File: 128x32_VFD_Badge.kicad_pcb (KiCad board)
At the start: 2 copper layers, 94 x 34.3 mm, 71 parts, among them J1 USB_C_Receptacle_USB2.0_16P, J2 Micro_SD_Card_Det2, Q1 CMSN3416K-HF, Q2 CMSN3416K-HF, SW1 SKRKAEE020, SW2 SKRKAEE020, SW3 SKRKAEE020, U1 USBLC6-2SC6, U2 TPS61391, U3 SN6507DGQ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

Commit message: Rev 0.1
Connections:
- D2 pad 1: (no net) -> GND
- D2 pad 2: GND -> (no net)
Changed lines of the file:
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@@
 			(layers "B.Cu" "B.Paste" "B.Mask")
 			(roundrect_rratio 0.25)
+			(net 1 "GND")
+			(pinfunction "A")
+			(pintype "passive")
 		)
 		(pad "2" smd roundrect
@@
 			(layers "B.Cu" "B.Paste" "B.Mask")
 			(roundrect_rratio 0.25)
-			(net 1 "GND")
-			(pinfunction "A")
-			(pintype "passive")
 		)
 		(pad "3" smd roundrect

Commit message: bitbanging
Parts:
- turned TR1 to 90 degrees
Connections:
- TR1 pad 1: /Controller & Display/Filament Driver/F1 -> Net-(U3-SW1)
- TR1 pad 2: Net-(D2-K) -> +3.3V
- TR1 pad 3: Net-(R8-Pad1) -> Net-(U3-SW2)
- TR1 pad 4: Net-(U3-SW1) -> /Controller & Display/Filament Driver/F1
- TR1 pad 5: +3.3V -> Net-(D2-K)
- TR1 pad 6: Net-(U3-SW2) -> Net-(R8-Pad1)
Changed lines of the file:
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@@
 		(property "Value" "+"
 			(at 4 -7 0)
-			(layer "B.Fab")
+			(layer "B.SilkS")
 			(effects
 				(font
@@
 		(property "Value" "-"
 			(at 4 -7 0)
-			(layer "B.Fab")
+			(layer "B.SilkS")
 			(effects
 				(font
@@
 	(footprint "Noritake:Transformer_Wuerth_750316888"
 		(layer "B.Cu")
-		(at 214.4 82 -90)
+		(at 214.4 82 90)
 		(descr "Power Transformer, horizontal core with bobbin, 6 pin, 2.54mm pitch, 11.24mm row spacing, 12.6x8.3x4.1mm")
 		(tags "transformer flyback")
@@
 		)
 		(property "Footprint" "Noritake:Transformer_Wuerth_750316888"
-			(at 0 0 90)
+			(at 0 0 -90)
 			(unlocked yes)
 			(layer "B.Fab")
@@
 		)
 		(property "Datasheet" "https://www.we-online.com/components/products/datasheet/750316888.pdf"
-			(at 0 0 90)
+			(at 0 0 -90)
 			(unlocked yes)
 			(layer "B.Fab")
@@
 		)
 		(property "Description" ""
-			(at 0 0 90)
+			(at 0 0 -90)
 			(unlocked yes)
 			(layer "B.Fab")
@@
 		(attr smd)
 		(fp_line
+			(start -5.6 -4.25)
+			(end 5.6 -4.25)
+			(stroke
+				(width 0.12)
+				(type solid)
+			)
+			(layer "B.SilkS")
+		)
+		(fp_line
 			(start 5.6 4.25)
 			(end -5.8 4.25)
-			(stroke
-				(width 0.12)
-				(type solid)
-			)
-			(layer "B.SilkS")
-		)
-		(fp_line
-			(start -5.6 -4.25)
-			(end 5.6 -4.25)
 			(stroke
 				(width 0.12)
@@
 		)
 		(fp_line
+			(start 7.8 -4.4)
+			(end 7.8 4.4)
+			(stroke
+				(width 0.05)
+				(type solid)
+			)
+			(layer "B.CrtYd")
+		)
+		(fp_line
+			(start -7.8 -4.4)
+			(end 7.8 -4.4)
+			(stroke
+				(width 0.05)
+				(type solid)
+			)
+			(layer "B.CrtYd")
+		)
+		(fp_line
+			(start 7.8 4.4)
+			(end -7.8 4.4)
+			(stroke
+				(width 0.05)
+				(type solid)
+			)
+			(layer "B.CrtYd")
+		)
+		(fp_line
 			(start -7.8 4.4)
 			(end -7.8 -4.4)
@@
 		)
 		(fp_line
-			(start 7.8 4.4)
-			(end -7.8 4.4)
-			(stroke
-				(width 0.05)
-				(type solid)
-			)
-			(layer "B.CrtYd")
-		)
-		(fp_line
-			(start -7.8 -4.4)
-			(end 7.8 -4.4)
-			(stroke
-				(width 0.05)
-				(type solid)
-			)
-			(layer "B.CrtYd")
-		)
-		(fp_line
-			(start 7.8 -4.4)
-			(end 7.8 4.4)
-			(stroke
-				(width 0.05)
-				(type solid)
-			)
-			(layer "B.CrtYd")
+			(start 5.715 -4.15)
+			(end 5.715 4.15)
+			(stroke
+				(width 0.1)
+				(type solid)
+			)
+			(layer "B.Fab")
+		)
+		(fp_line
+			(start -5.715 -4.15)
+			(end 5.715 -4.15)
+			(stroke
+				(width 0.1)
+				(type solid)
+			)
+			(layer "B.Fab")
+		)
+		(fp_line
+			(start -5.715 3.1)
+			(end -5.715 -4.15)
+			(stroke
+				(width 0.1)
+				(type solid)
+			)
+			(layer "B.Fab")
+		)
+		(fp_line
+			(start 5.715 4.15)
+			(end -4.7025 4.15)
+			(stroke
+				(width 0.1)
+				(type solid)
+			)
+			(layer "B.Fab")
 		)
 		(fp_line
@@
 			(layer "B.Fab")
 		)
-		(fp_line
-			(start 5.715 4.15)
-			(end -4.7025 4.15)
-			(stroke
-				(width 0.1)
-				(type solid)
-			)
-			(layer "B.Fab")
-		)
-		(fp_line
-			(start -5.715 3.1)
-			(end -5.715 -4.15)
-			(stroke
-				(width 0.1)
-				(type solid)
-			)
-			(layer "B.Fab")
-		)
-		(fp_line
-			(start -5.715 -4.15)
-			(end 5.715 -4.15)
-			(stroke
-				(width 0.1)
-				(type solid)
-			)
-			(layer "B.Fab")
-		)
-		(fp_line
-			(start 5.715 -4.15)
-			(end 5.715 4.15)
-			(stroke
-				(width 0.1)
-				(type solid)
-			)
-			(layer "B.Fab")
-		)
 		(fp_text user "${REFERENCE}"
 			(at 0 0 90)
@@
 		)
 		(pad "1" smd roundrect
-			(at -6.715 2.54 270)
+			(at -6.715 2.54 90)
+			(size 1.82 1.22)
+			(layers "B.Cu" "B.Paste" "B.Mask")
+			(roundrect_rratio 0.05)
+			(net 78 "Net-(U3-SW1)")
+			(pintype "passive")
+		)
+		(pad "2" smd roundrect
+			(at -6.715 0 90)
+			(size 1.82 1.22)
+			(layers "B.Cu" "B.Paste" "B.Mask")
+			(roundrect_rratio 0.05)
+			(net 3 "+3.3V")
+			(pintype "passive")
+		)
+		(pad "3" smd roundrect
+			(at -6.715 -2.54 90)
+			(size 1.82 1.22)
+			(layers "B.Cu" "B.Paste" "B.Mask")
+			(roundrect_rratio 0.05)
+			(net 77 "Net-(U3-SW2)")
+			(pintype "passive")
+		)
+		(pad "4" smd roundrect
+			(at 6.715 -2.54 90)
 			(size 1.82 1.22)
 			(layers "B.Cu" "B.Paste" "B.Mask")
@@
 			(pintype "passive")
 		)
-		(pad "2" smd roundrect
-			(at -6.715 0 270)
+		(pad "5" smd roundrect
+			(at 6.715 0 90)
 			(size 1.82 1.22)
 			(layers "B.Cu" "B.Paste" "B.Mask")
@@
 			(pintype "passive")
 		)
-		(pad "3" smd roundrect
-			(at -6.715 -2.54 270)
+		(pad "6" smd roundrect
+			(at 6.715 2.54 90)
 			(size 1.82 1.22)
 			(layers "B.Cu" "B.Paste" "B.Mask")
@@
 			(pintype "passive")
 		)
-		(pad "4" smd roundrect
-			(at 6.715 -2.54 270)
-			(size 1.82 1.22)
-			(layers "B.Cu" "B.Paste" "B.Mask")
-			(roundrect_rratio 0.05)
-			(net 78 "Net-(U3-SW1)")
-			(pintype "passive")
-		)
-		(pad "5" smd roundrect
-			(at 6.715 0 270)
-			(size 1.82 1.22)
-			(layers "B.Cu" "B.Paste" "B.Mask")
-			(roundrect_rratio 0.05)
-			(net 3 "+3.3V")
-			(pintype "passive")
-		)
-		(pad "6" smd roundrect
-			(at 6.715 2.54 270)
-			(size 1.82 1.22)
-			(layers "B.Cu" "B.Paste" "B.Mask")
-			(roundrect_rratio 0.05)
-			(net 77 "Net-(U3-SW2)")
-			(pintype "passive")
-		)

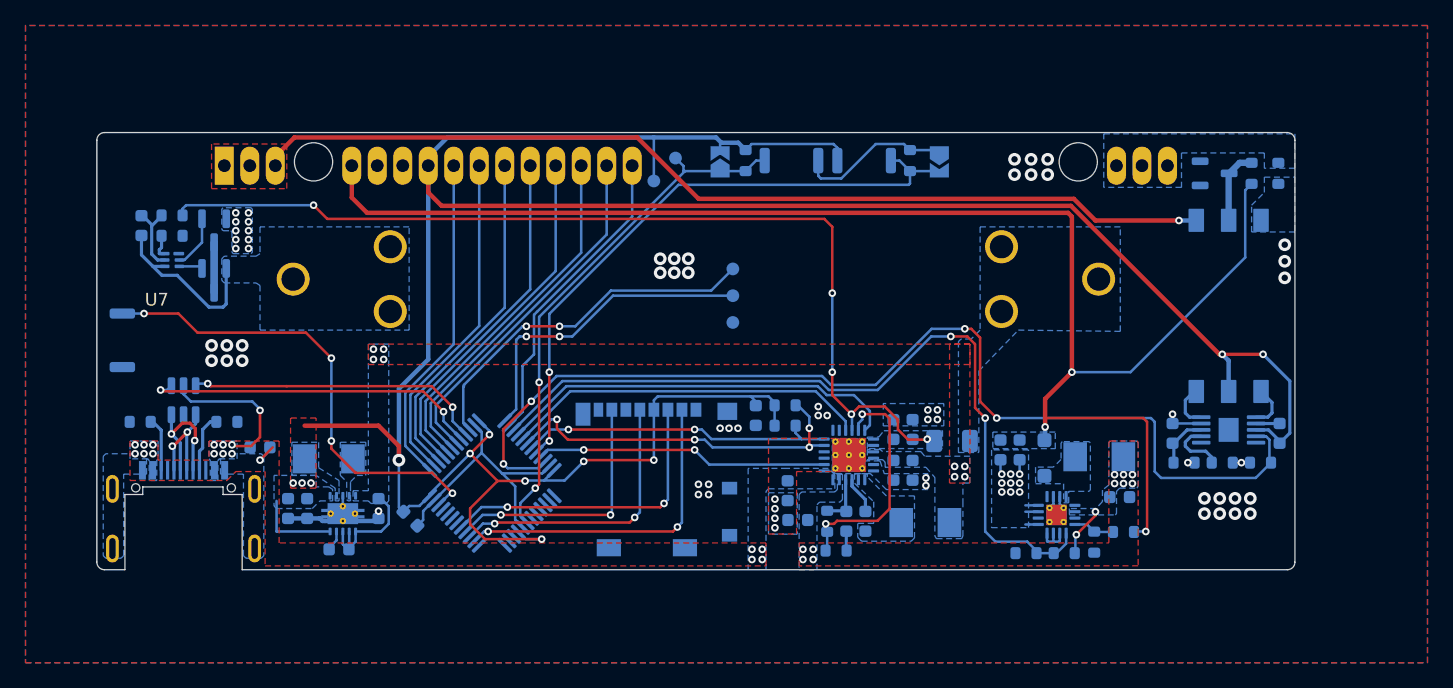
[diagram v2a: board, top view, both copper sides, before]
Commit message: spi_pins
VFD over SPI
3.3V and 5V over P-Channel Mosfet
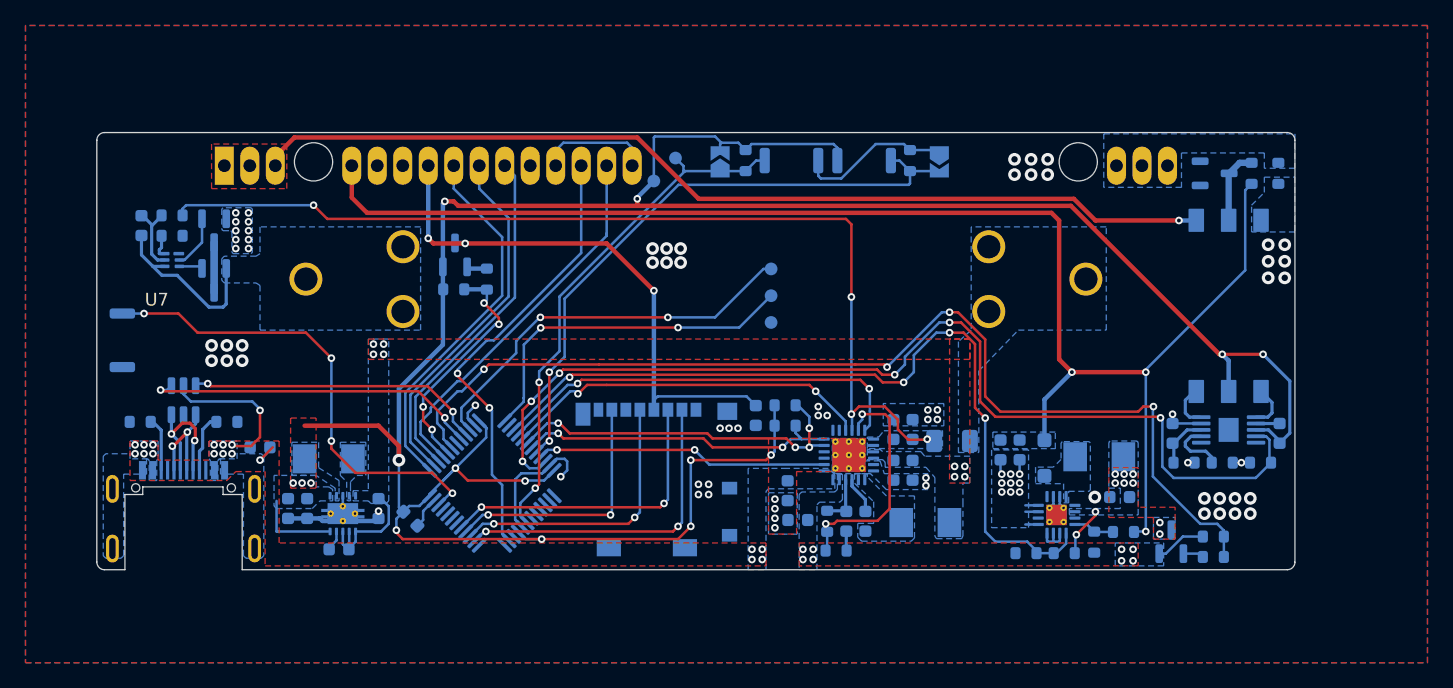
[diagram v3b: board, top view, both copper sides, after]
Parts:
- added Q5: IRLML6401, Package_TO_SOT_SMD:SOT-23, B.Cu at (209.9, 100.5)
- added Q6: IRLML6401, Package_TO_SOT_SMD:SOT-23, B.Cu at (153.7, 78.0)
- added R20: 10k, Resistor_SMD:R_0603_1608Metric, B.Cu at (213.2, 100.1)
- added R21: 10k, Resistor_SMD:R_0603_1608Metric, B.Cu at (153.6, 80.7)
- added R22: 100R, Resistor_SMD:R_0603_1608Metric, B.Cu at (213.2, 101.7)
- added R23: 100R, Resistor_SMD:R_0603_1608Metric, B.Cu at (156.2, 79.9)
- moved TP2 3.00 mm to (178.5, 83.3)
- moved TP4 3.00 mm to (178.5, 79.1)
- moved TP5 3.00 mm to (178.5, 81.2)
- moved BAT1 1.00 mm to (203.2, 79.9)
- moved BAT2 1.00 mm to (142.0, 79.9)
- turned C2 to 180 degrees
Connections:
- C2 pad 1: VPMID_5V -> /Controller & Display/5V_SWITCHED
- C21 pad 1: +3.3V -> /Controller & Display/3.3V_SWITCHED
- J2 pad 4: +3.3V -> /Controller & Display/3.3V_SWITCHED
- L1 pad 1: VPMID_5V -> /Controller & Display/5V_SWITCHED
- R4 pad 1: VPMID_5V -> /Controller & Display/5V_SWITCHED
- U2 pad 10: VPMID_5V -> /Controller & Display/5V_SWITCHED
- U7 pad 14: /Controller & Display/SOUT1 -> /Controller & Display/SIN2
- U7 pad 9: +3.3V -> /Controller & Display/3.3V_SWITCHED
- U8 pad 11: unconnected-(U8-PA1-Pad11) -> /Controller & Display/CLK
- U8 pad 28: /Controller & Display/SOUT2 -> /Controller & Display/SIN1
- U8 pad 29: /Controller & Display/SOUT1 -> /Controller & Display/~{3.3V_EN}
- U8 pad 30: /Controller & Display/CLK -> /Controller & Display/~{5V_EN}
- U8 pad 31: /Controller & Display/SIN1 -> unconnected-(U8-PA10-Pad31)
- U8 pad 38: /Controller & Display/SIN2 -> unconnected-(U8-PA15-Pad38)
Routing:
- net /Controller & Display/~{5V_EN}: track 0.00 -> 83.8 mm, vias 0 -> 4
- net /Controller & Display/3.3V_SWITCHED: track 0.00 -> 46.8 mm, vias 0 -> 3
- net /Controller & Display/SOUT1: track 27.4 -> 0.00 mm
- net /Controller & Display/SOUT2: track 27.1 -> 1.10 mm
- net /Controller & Display/~{3.3V_EN}: track 0.00 -> 18.5 mm, vias 0 -> 4
- net /Controller & Display/SIN2: track 24.4 -> 9.01 mm
- net +3.3V: track 227.9 -> 212.8 mm, vias 12 -> 15
- net /Controller & Display/CLK: track 27.7 -> 35.5 mm, vias 0 -> 2
- net GND: track 63.8 -> 57.4 mm, vias 72 -> 78
- net +45V: track 119.1 -> 115.0 mm
- net /Controller & Display/5V_SWITCHED: track 0.00 -> 3.84 mm, vias 0 -> 10
- net /Controller & Display/BLK: track 26.3 -> 29.4 mm
- net /Controller & Display/SWDIO: track 28.6 -> 31.4 mm
- net /Controller & Display/SWCLK: track 25.2 -> 27.6 mm
- net /Controller & Display/FIL_EN: track 84.0 -> 82.0 mm, vias 4 -> 6
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- added copper zone on B.Cu, net /Controller & Display/5V_SWITCHED
- added copper zone on F.Cu, net /Controller & Display/5V_SWITCHED
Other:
- board text added: "128x32 VFD Badge Rev. 0.2, July 2025 J.Radtke - radtke.dk"
- board text removed: "128x32 VFD Badge Rev. 0.1, May 2025 J.Radtke - radtke.dk"
